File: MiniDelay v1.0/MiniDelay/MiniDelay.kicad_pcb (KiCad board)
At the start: 2 copper layers, 52 parts, among them J1 IDC_2x05, U1 TL074, U2 PT2399

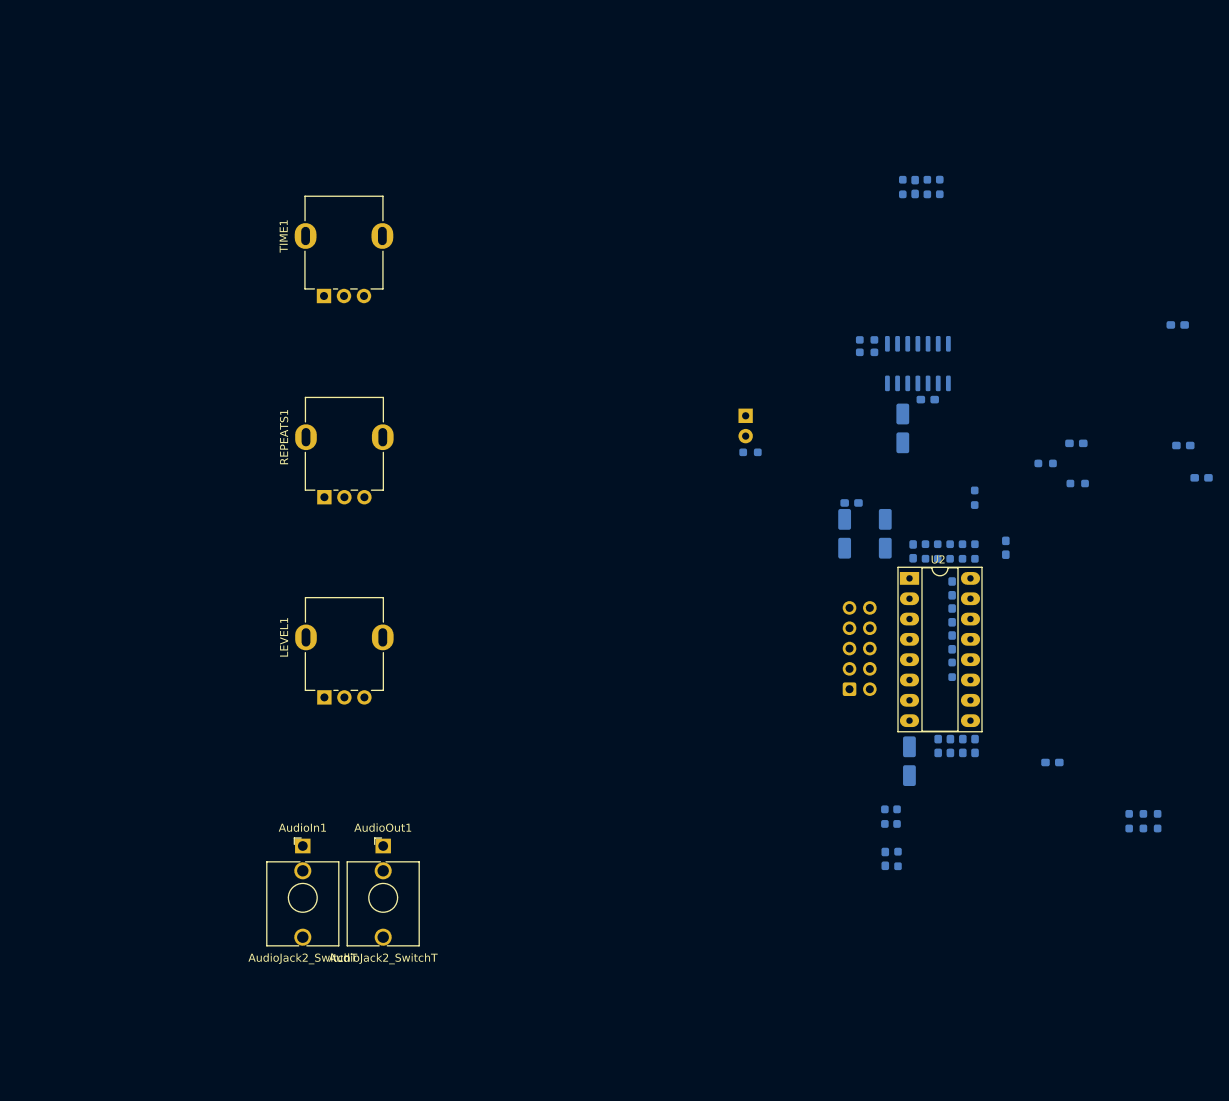
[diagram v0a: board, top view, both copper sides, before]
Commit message: Moved everything to SMD
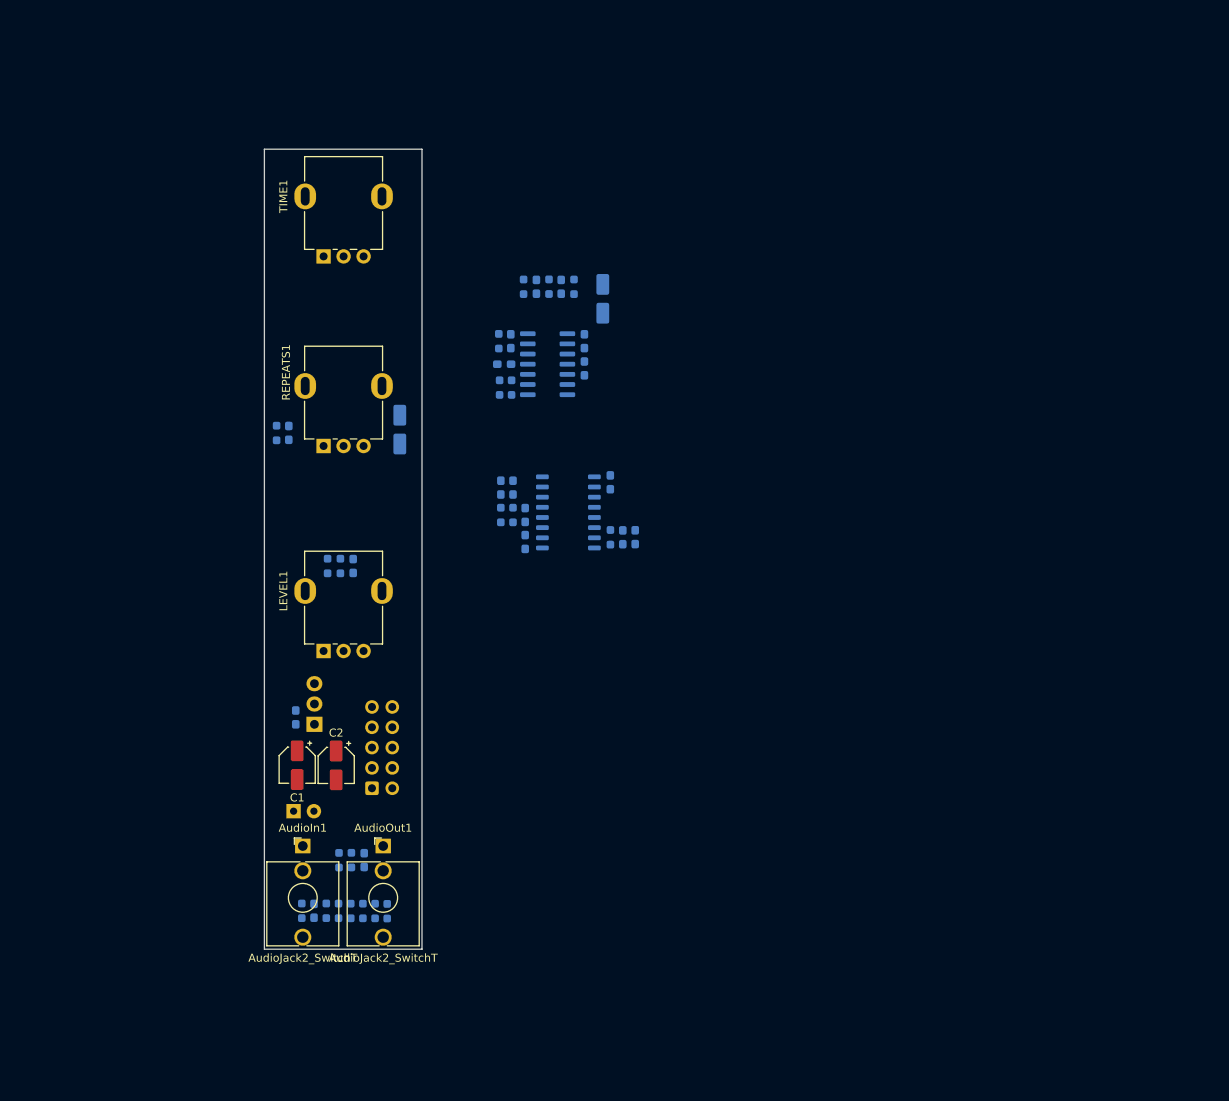
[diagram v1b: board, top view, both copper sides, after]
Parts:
- added U3: L7805, Package_TO_SOT_THT:TO-220-3_Vertical, B.Cu at (117.3, 128.5)
- C1, C2: moved to F.Cu
- U2: footprint Package_DIP:DIP-16_W7.62mm_Socket_LongPads -> Package_SO:SOP-16_4.55x10.3mm_P1.27mm; moved to B.Cu
- moved R9 113.9 mm to (126.3, 151.8), turned to 90 degrees
- moved R18 113.8 mm to (121.8, 151.8)
- moved C3 103.4 mm to (114.9, 127.6), turned to 90 degrees
- moved R11 100.9 mm to (121.9, 145.5), turned to 90 degrees
- moved R16 100.3 mm to (112.5, 92.1), turned to -90 degrees
- moved R6 96.7 mm to (124.8, 151.8)
- moved R4 96.4 mm to (123.3, 151.8)
- moved C12 89.2 mm to (123.5, 145.5)
- moved C21 87.0 mm to (140.6, 98.9), turned to 90 degrees
- moved C10 86.0 mm to (114.0, 92.1)
- moved C19 84.0 mm to (142.1, 98.9), turned to -90 degrees
- moved C20 83.5 mm to (148.1, 73.8), turned to -90 degrees
- moved C16 80.9 mm to (122.1, 108.7), turned to -90 degrees
- moved R10 79.1 mm to (118.9, 108.7), turned to -90 degrees
- moved C7 76.0 mm to (127.9, 91.7), turned to 90 degrees
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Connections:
- C1 pad 1: Net-(C1-Pad1) -> +12V
- C2 pad 2: Net-(C2-Pad2) -> -12V
- C3 pad 1: Net-(C1-Pad1) -> +12V
- C4 pad 2: Net-(C2-Pad2) -> -12V
- R2 pad 2: Net-(C1-Pad1) -> +12V
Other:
- board outline added: 19.7 x 100 mm

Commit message: Updated bom using LCSC
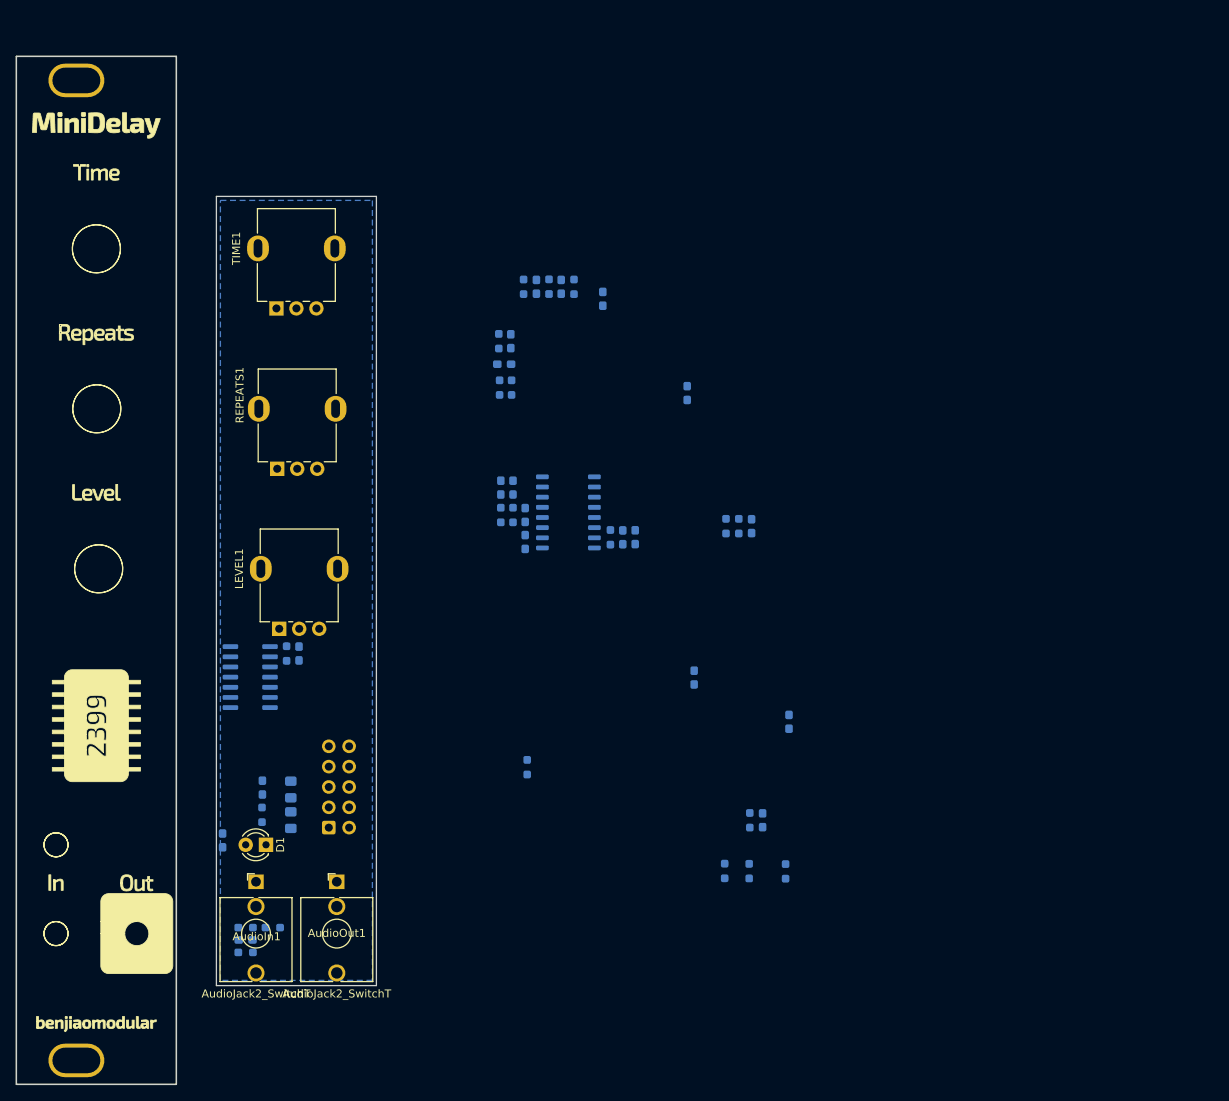
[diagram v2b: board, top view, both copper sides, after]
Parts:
- removed U3: L7805, Package_TO_SOT_THT:TO-220-3_Vertical
- added REF**: Panel_4HP, benjiaomodular:Panel_4HP, F.Cu at (80.0, 45.0)
- C1, C2: value 100uF -> 22uF; footprint Capacitor_SMD:CP_Elec_4x3.9 -> Capacitor_SMD:C_0805_2012Metric_Pad1.18x1.45mm_HandSolder; moved to B.Cu
- C11, C13: value 100nf -> 100nF
- C18, C7: footprint Capacitor_SMD:CP_Elec_4x3.9 -> Capacitor_SMD:C_0603_1608Metric_Pad1.08x0.95mm_HandSolder
- D1: moved to F.Cu
- moved C14 74.3 mm to (105.8, 143.0)
- moved C7 60.8 mm to (176.6, 128.2), turned to -90 degrees
- moved C17 57.9 mm to (110.8, 136.4)
- moved U1 54.0 mm to (109.2, 122.6)
- moved C6 52.9 mm to (115.3, 119.6)
- moved R16 52.2 mm to (143.8, 133.8)
- moved C12 50.0 mm to (173.3, 140.5)
- moved C16 50.0 mm to (171.9, 103.7)
- moved R11 50.0 mm to (171.7, 140.5)
- moved R8 50.0 mm to (170.3, 103.7)
- moved R9 50.0 mm to (176.2, 146.9)
- moved C10 50.0 mm to (163.8, 87.1)
- moved C3 50.0 mm to (164.7, 122.6)
- moved R17 50.0 mm to (168.5, 146.8)
- moved R18 50.0 mm to (171.6, 146.8)
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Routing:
- added copper zone on B.Cu, net GND
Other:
- board size 19.7 x 100 mm -> 45 x 128.5 mm

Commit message: Worked on BOM
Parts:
- added REF**: PanelHole_Potentiometer_RV09, benjiaomodular:PanelHole_Potentiometer_RV09, F.Cu at (107.5, 91.5)
- added REF**: PanelHole_Potentiometer_RV09, benjiaomodular:PanelHole_Potentiometer_RV09, F.Cu at (107.5, 71.5)
- added REF**: PanelHole_AudioJack_3.5mm, benjiaomodular:PanelHole_AudioJack_3.5mm, F.Cu at (105.0, 143.2)
- added REF**: PanelHole_AudioJack_3.5mm, benjiaomodular:PanelHole_AudioJack_3.5mm, F.Cu at (115.0, 143.2)
- added REF**: PanelHole_Potentiometer_RV09, benjiaomodular:PanelHole_Potentiometer_RV09, F.Cu at (107.5, 111.5)
- added U3: L7805, Package_TO_SOT_SMD:TO-252-2, B.Cu at (131.7, 123.5)
- moved C7 71.6 mm to (129.9, 73.8)
- moved R11 63.1 mm to (129.5, 93.5), turned to 0 degrees
- moved C12 63.1 mm to (129.5, 95.1), turned to 0 degrees
- moved R9 56.7 mm to (144.0, 100.2)
- moved R6 51.6 mm to (133.8, 107.1)
- moved R18 51.1 mm to (137.2, 109.1), turned to 0 degrees
- moved R17 50.6 mm to (137.2, 107.1), turned to 0 degrees
- moved C9 43.9 mm to (136.6, 66.4), turned to 0 degrees
- moved C16 43.8 mm to (143.9, 70.0)
- moved R10 42.8 mm to (142.3, 70.0)
- moved C8 41.8 mm to (136.6, 67.9), turned to 0 degrees
- moved R16 41.3 mm to (144.1, 92.6), turned to 90 degrees
- moved R5 39.8 mm to (136.6, 69.5), turned to 180 degrees
- moved R8 37.3 mm to (137.4, 86.1)
- moved U1 36.0 mm to (134.9, 97.3)
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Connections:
- U1 pad 1: Net-(C6-Pad1) -> Net-(LEVEL1-Pad3)
- U1 pad 10: Net-(C21-Pad2) -> GND
- U1 pad 12: GND -> Net-(C12-Pad2)
- U1 pad 13: Net-(C22-Pad2) -> Net-(C18-Pad2)
- U1 pad 14: Net-(C22-Pad1) -> Net-(C18-Pad2)
- U1 pad 2: Net-(C6-Pad2) -> Net-(R19-Pad2)
- U1 pad 3: GND -> Net-(C21-Pad2)
- U1 pad 5: Net-(C12-Pad2) -> GND
- U1 pad 6: Net-(C18-Pad2) -> Net-(C22-Pad2)
- U1 pad 7: Net-(C18-Pad2) -> Net-(C22-Pad1)
- U1 pad 8: Net-(LEVEL1-Pad3) -> Net-(C6-Pad1)
- U1 pad 9: Net-(R19-Pad2) -> Net-(C6-Pad2)
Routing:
- net Net-(C6-Pad2): track 0.00 -> 61.9 mm
- net +12V: track 0.00 -> 58.8 mm, vias 0 -> 1
- net +5V: track 0.00 -> 58.3 mm, vias 0 -> 2
- net -12V: track 0.00 -> 56.9 mm, vias 0 -> 1
- net Net-(AudioOut1-PadT): track 0.00 -> 55.5 mm
- net DRY_OUT: track 0.00 -> 53.0 mm
- net Net-(LEVEL1-Pad3): track 0.00 -> 26.3 mm
- net Net-(C16-Pad2): track 0.00 -> 25.7 mm
- net Net-(C19-Pad2): track 0.00 -> 19.2 mm
- net Net-(C22-Pad2): track 0.00 -> 17.3 mm
- net REPEATS: track 0.00 -> 16.7 mm, vias 0 -> 1
- net Net-(C6-Pad1): track 0.00 -> 15.0 mm
- net Net-(C11-Pad2): track 0.00 -> 13.1 mm
- net Net-(C20-Pad1): track 0.00 -> 11.9 mm
- net Net-(C9-Pad2): track 0.00 -> 9.35 mm
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- added copper zone on B.Cu, net (none)
- added copper zone on F.Cu, net (none)
- added copper zone on F.Cu, net GND
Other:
- board text added: "MiniDelay v1.0"
- board text added: "by benjiaomodular"
